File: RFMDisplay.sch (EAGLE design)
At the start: 16 parts, among them IC1 74HCT595N, IC2 74HCT595N, IC3 74HCT595N, IC4 74HCT595N

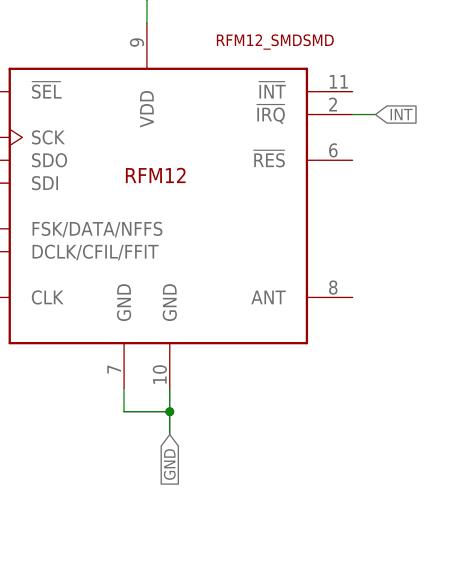
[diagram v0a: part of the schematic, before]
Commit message: Adjusted some wire widths
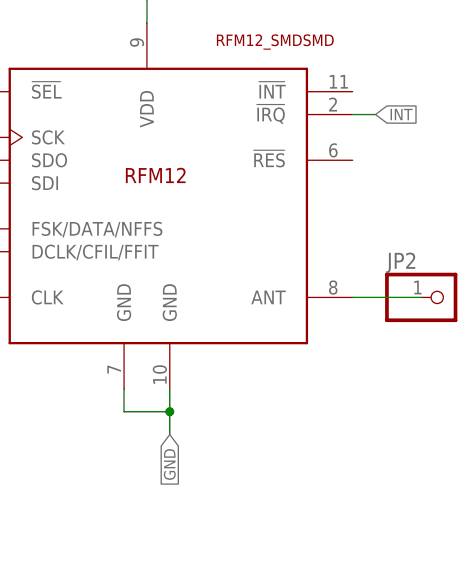
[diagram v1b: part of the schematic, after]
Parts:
- added JP2: (no value), pinhead:PINHD-1X1
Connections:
- new net N$33: JP2.1, U$2.ANT
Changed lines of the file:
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@@
 <part name="U$2" library="rfm_12" deviceset="RFM12_SMD" device="SMD"/>
 <part name="BAT1" library="sn2032" deviceset="SN2032" device=""/>
+<part name="JP2" library="pinhead" deviceset="PINHD-1X1" device=""/>
 </parts>
 <sheets>
@@
 <instance part="U$2" gate="U$1" x="345.44" y="17.78"/>
 <instance part="BAT1" gate="1" x="287.02" y="-12.7"/>
+<instance part="JP2" gate="G$1" x="378.46" y="12.7"/>
 </instances>
 <busses>
@@
 </segment>
 </net>
+<net name="N$33" class="0">
+<segment>
+<pinref part="U$2" gate="U$1" pin="ANT"/>
+<wire x1="368.3" y1="12.7" x2="375.92" y2="12.7" width="0.1524" layer="91"/>
+<pinref part="JP2" gate="G$1" pin="1"/>
+</segment>
+</net>
